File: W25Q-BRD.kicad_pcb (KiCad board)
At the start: 2 copper layers, 16 x 23 mm, 7 parts, among them J1 QSPI, U1 W25Q128JVSIQ

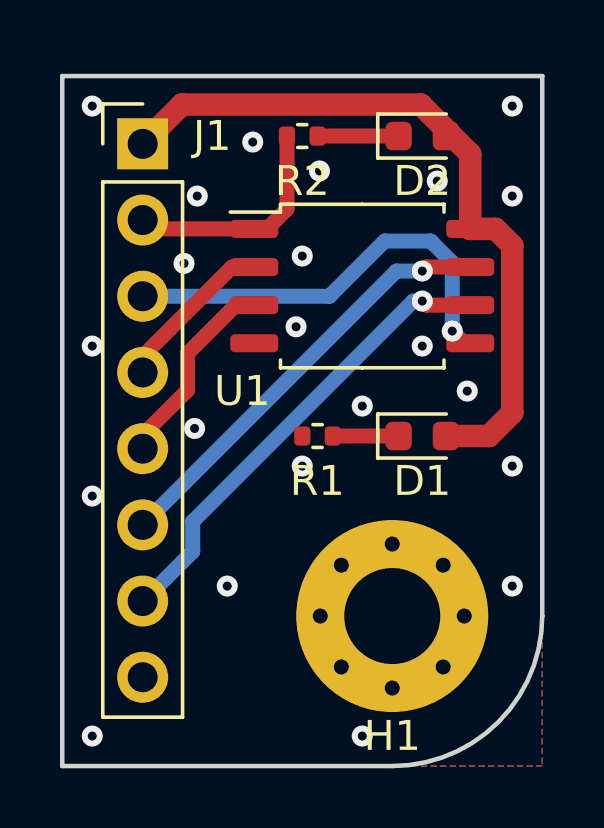
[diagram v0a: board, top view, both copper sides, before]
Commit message: Moved some components around. Generated CAM files.
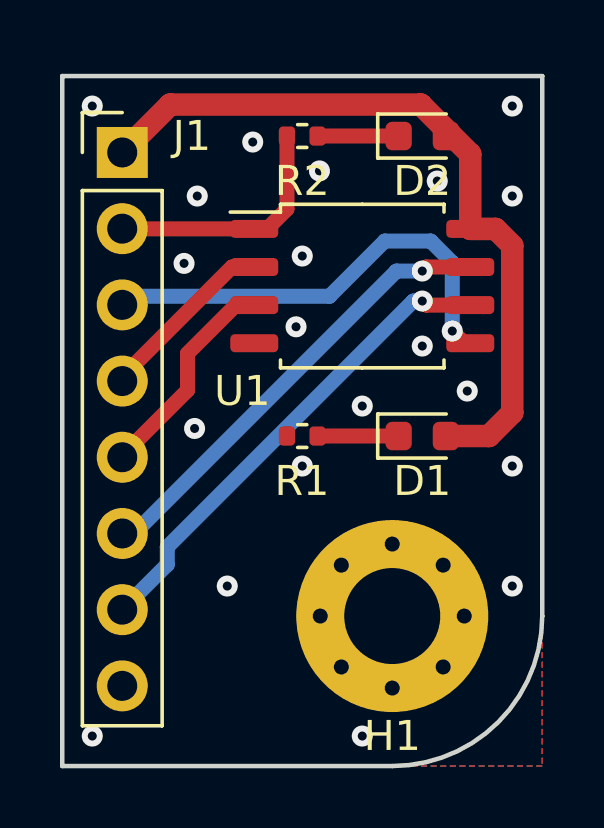
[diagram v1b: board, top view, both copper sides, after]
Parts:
- moved J1 0.74 mm to (133.0, 96.5)
- moved R1 0.51 mm to (139.0, 106.0)
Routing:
- net /IO3: track 14.5 -> 15.3 mm
- net /IO0: track 14.4 -> 15.2 mm
- net +3.3V: track 24.4 -> 25.2 mm
- net /IO1: track 5.49 -> 6.06 mm
- net /IO2: track 6.68 -> 7.25 mm
- net /NCS: track 7.64 -> 8.20 mm
- net /CLK: track 15.7 -> 16.3 mm
- net Net-(D1-Pad1): track 2.19 -> 2.70 mm
- net GND: vias 22 -> 20
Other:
- board text added: "3V3"
- board text added: "CLK"
- board text added: "GND"
- board text added: "IO0"
- board text added: "IO1"
- board text added: "IO2"
- board text added: "IO3"
- board text added: "NCS"
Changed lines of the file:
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@@
   )
   (footprint "Resistor_SMD:R_0402_1005Metric" (layer "F.Cu")
-    (at 139.51 106 180)
+    (at 139 106 180)
     (descr "Resistor SMD 0402 (1005 Metric), square (rectangular) end terminal, IPC_7351 nominal, (Body size source: IPC-SM-782 page 72, https://www.pcb-3d.com/wordpress/wp-content/uploads/ipc-sm-782a_amendment_1_and_2.pdf), generated with kicad-footprint-generator")
     (tags "resistor")
@@
       (effects (font (size 1 1) (thickness 0.15)))
     )
-    (fp_text user "${REFERENCE}" (at 0 0) (layer "F.Fab")
+    (fp_text user "${REFERENCE}" (at 0.51 0) (layer "F.Fab")
       (effects (font (size 0.26 0.26) (thickness 0.04)))
     )
@@
   )
   (footprint "Connector_PinHeader_2.54mm:PinHeader_1x08_P2.54mm_Vertical" (layer "F.Cu")
-    (at 133.68 96.26)
+    (at 133 96.547158)
     (descr "Through hole straight pin header, 1x08, 2.54mm pitch, single row")
     (tags "Through hole pin header THT 1x08 2.54mm single row")
@@
     (property "Sheetname" "")
     (attr through_hole)
-    (fp_text reference "J1" (at 2.32 -0.26) (layer "F.SilkS")
+    (fp_text reference "J1" (at 2.32 -0.547158) (layer "F.SilkS")
       (effects (font (size 1 1) (thickness 0.15)))
     )
@@
   (gr_arc (start 147 112) (mid 145.535534 115.535534) (end 142 117) (layer "Edge.Cuts") (width 0.15))
   (gr_line (start 147 94) (end 131 94) (layer "Edge.Cuts") (width 0.15))
-  (gr_text "${TITLE}\n${COMPANY}" (at 141 102 270) (layer "B.SilkS")
-    (effects (font (size 1 1) (thickness 0.15)) (justify mirror))
-  )
-  (segment (start 142.2125 106) (end 140.02 106) (width 0.5) (layer "F.Cu") (net 1))
-  (segment (start 142.95 94.95) (end 134.99 94.95) (width 0.75) (layer "F.Cu") (net 2))
+  (gr_text "IO2" (at 136 106.707158) (layer "B.SilkS")
+    (effects (font (size 1 1) (thickness 0.15)) (justify mirror))
+  )
+  (gr_text "IO0" (at 136 101.627158) (layer "B.SilkS")
+    (effects (font (size 1 1) (thickness 0.15)) (justify mirror))
+  )
+  (gr_text "NCS" (at 136 99.087158) (layer "B.SilkS")
+    (effects (font (size 1 1) (thickness 0.15)) (justify mirror))
+  )
+  (gr_text "IO3" (at 136 109.247158) (layer "B.SilkS")
+    (effects (font (size 1 1) (thickness 0.15)) (justify mirror))
+  )
+  (gr_text "GND" (at 136 114.327158) (layer "B.SilkS")
+    (effects (font (size 1 1) (thickness 0.15)) (justify mirror))
+  )
+  (gr_text "${TITLE}\n${COMPANY}" (at 144.5 102 90) (layer "B.SilkS")
+    (effects (font (size 1 1) (thickness 0.15)) (justify mirror))
+  )
+  (gr_text "IO1" (at 136 104.167158) (layer "B.SilkS")
+    (effects (font (size 1 1) (thickness 0.15)) (justify mirror))
+  )
+  (gr_text "3V3" (at 136 96.547158) (layer "B.SilkS")
+    (effects (font (size 1 1) (thickness 0.15)) (justify mirror))
+  )
+  (gr_text "CLK" (at 136 111.787158) (layer "B.SilkS")
+    (effects (font (size 1 1) (thickness 0.15)) (justify mirror))
+  )
+  (segment (start 142.2125 106) (end 139.51 106) (width 0.5) (layer "F.Cu") (net 1))
   (segment (start 146 105.225) (end 146 99.65) (width 0.75) (layer "F.Cu") (net 2))
   (segment (start 145.445 99.095) (end 144.6 99.095) (width 0.75) (layer "F.Cu") (net 2))
-  (segment (start 144.6 99.095) (end 144.6 96.6) (width 0.75) (layer "F.Cu") (net 2))
   (segment (start 145.225 106) (end 146 105.225) (width 0.75) (layer "F.Cu") (net 2))
-  (segment (start 134.99 94.95) (end 133.68 96.26) (width 0.75) (layer "F.Cu") (net 2))
+  (segment (start 133 96.547158) (end 134.597158 94.95) (width 0.75) (layer "F.Cu") (net 2))
   (segment (start 146 99.65) (end 145.445 99.095) (width 0.75) (layer "F.Cu") (net 2))
+  (segment (start 144.6 96.6) (end 144.6 99.095) (width 0.75) (layer "F.Cu") (net 2))
+  (segment (start 142.95 94.95) (end 144.6 96.6) (width 0.75) (layer "F.Cu") (net 2))
+  (segment (start 134.597158 94.95) (end 142.95 94.95) (width 0.75) (layer "F.Cu") (net 2))
   (segment (start 143.7875 106) (end 145.225 106) (width 0.75) (layer "F.Cu") (net 2))
-  (segment (start 144.6 96.6) (end 142.95 94.95) (width 0.75) (layer "F.Cu") (net 2))
   (segment (start 142.2125 96) (end 139.51 96) (width 0.5) (layer "F.Cu") (net 3))
   (via (at 143 103) (size 0.7) (drill 0.3) (layers "F.Cu" "B.Cu") (free) (net 4))
@@
   (via (at 146 95) (size 0.7) (drill 0.3) (layers "F.Cu" "B.Cu") (free) (net 4))
   (via (at 144.5 104.5) (size 0.7) (drill 0.3) (layers "F.Cu" "B.Cu") (free) (net 4))
-  (via (at 132 108) (size 0.7) (drill 0.3) (layers "F.Cu" "B.Cu") (free) (net 4))
   (via (at 132 116) (size 0.7) (drill 0.3) (layers "F.Cu" "B.Cu") (free) (net 4))
   (via (at 137.349245 96.200026) (size 0.7) (drill 0.3) (layers "F.Cu" "B.Cu") (free) (net 4))
   (via (at 135.060021 100.245189) (size 0.7) (drill 0.3) (layers "F.Cu" "B.Cu") (free) (net 4))
   (via (at 141 105) (size 0.7) (drill 0.3) (layers "F.Cu" "B.Cu") (free) (net 4))
-  (via (at 132 103) (size 0.7) (drill 0.3) (layers "F.Cu" "B.Cu") (free) (net 4))
   (via (at 143.5 97.5) (size 0.7) (drill 0.3) (layers "F.Cu" "B.Cu") (free) (net 4))
   (via (at 146 107) (size 0.7) (drill 0.3) (layers "F.Cu" "B.Cu") (free) (net 4))
@@
   (segment (start 143 101.5) (end 143.135 101.635) (width 0.5) (layer "F.Cu") (net 5))
   (via (at 143 101.5) (size 0.7) (drill 0.3) (layers "F.Cu" "B.Cu") (net 5))
-  (segment (start 135.35 108.85) (end 135.35 109.85) (width 0.5) (layer "B.Cu") (net 5))
+  (segment (start 134.5 109.7) (end 134.5 110.287158) (width 0.5) (layer "B.Cu") (net 5))
+  (segment (start 134.5 110.287158) (end 133 111.787158) (width 0.5) (layer "B.Cu") (net 5))
+  (segment (start 142.7 101.5) (end 134.5 109.7) (width 0.5) (layer "B.Cu") (net 5))
   (segment (start 143 101.5) (end 142.7 101.5) (width 0.5) (layer "B.Cu") (net 5))
-  (segment (start 133.7 111.5) (end 133.68 111.5) (width 0.5) (layer "B.Cu") (net 5))
-  (segment (start 135.35 109.85) (end 133.7 111.5) (width 0.5) (layer "B.Cu") (net 5))
-  (segment (start 142.7 101.5) (end 135.35 108.85) (width 0.5) (layer "B.Cu") (net 5))
   (segment (start 144 102.5) (end 144.405 102.905) (width 0.5) (layer "F.Cu") (net 6))
   (segment (start 144.405 102.905) (end 144.6 102.905) (width 0.5) (layer "F.Cu") (net 6))
   (via (at 144 102.5) (size 0.7) (drill 0.3) (layers "F.Cu" "B.Cu") (net 6))
+  (segment (start 133.287158 101.34) (end 133 101.627158) (width 0.5) (layer "B.Cu") (net 6))
   (segment (start 143.282843 99.5) (end 141.75 99.5) (width 0.5) (layer "B.Cu") (net 6))
+  (segment (start 144 102.5) (end 144 100.217157) (width 0.5) (layer "B.Cu") (net 6))
   (segment (start 141.75 99.5) (end 139.91 101.34) (width 0.5) (layer "B.Cu") (net 6))
-  (segment (start 139.91 101.34) (end 133.68 101.34) (width 0.5) (layer "B.Cu") (net 6))
   (segment (start 144 100.217157) (end 143.282843 99.5) (width 0.5) (layer "B.Cu") (net 6))
-  (segment (start 144 102.5) (end 144 100.217157) (width 0.5) (layer "B.Cu") (net 6))
-  (segment (start 133.68 103.345) (end 133.68 103.88) (width 0.5) (layer "F.Cu") (net 7))
-  (segment (start 136.66 100.365) (end 133.68 103.345) (width 0.5) (layer "F.Cu") (net 7))
-  (segment (start 137.4 100.365) (end 136.66 100.365) (width 0.5) (layer "F.Cu") (net 7))
-  (segment (start 137.4 101.635) (end 136.79 101.635) (width 0.5) (layer "F.Cu") (net 8))
-  (segment (start 135.175 103.25) (end 135.175 104.475) (width 0.5) (layer "F.Cu") (net 8))
-  (segment (start 136.79 101.635) (end 135.175 103.25) (width 0.5) (layer "F.Cu") (net 8))
-  (segment (start 133.68 105.97) (end 133.68 106.42) (width 0.5) (layer "F.Cu") (net 8))
-  (segment (start 135.175 104.475) (end 133.68 105.97) (width 0.5) (layer "F.Cu") (net 8))
+  (segment (start 139.91 101.34) (end 133.287158 101.34) (width 0.5) (layer "B.Cu") (net 6))
+  (segment (start 136.66 100.365) (end 137.4 100.365) (width 0.5) (layer "F.Cu") (net 7))
+  (segment (start 133 104.025) (end 136.66 100.365) (width 0.5) (layer "F.Cu") (net 7))
+  (segment (start 133 104.167158) (end 133 104.025) (width 0.5) (layer "F.Cu") (net 7))
+  (segment (start 136.79 101.635) (end 137.4 101.635) (width 0.5) (layer "F.Cu") (net 8))
+  (segment (start 135.175 104.475) (end 135.175 103.25) (width 0.5) (layer "F.Cu") (net 8))
+  (segment (start 133 106.707158) (end 133 106.65) (width 0.5) (layer "F.Cu") (net 8))
+  (segment (start 133 106.65) (end 135.175 104.475) (width 0.5) (layer "F.Cu") (net 8))
+  (segment (start 135.175 103.25) (end 136.79 101.635) (width 0.5) (layer "F.Cu") (net 8))
   (segment (start 143.135 100.365) (end 144.6 100.365) (width 0.5) (layer "F.Cu") (net 9))
   (segment (start 143 100.5) (end 143.135 100.365) (width 0.5) (layer "F.Cu") (net 9))
   (via (at 143 100.5) (size 0.7) (drill 0.3) (layers "F.Cu" "B.Cu") (net 9))
-  (segment (start 142.14 100.5) (end 133.68 108.96) (width 0.5) (layer "B.Cu") (net 9))
+  (segment (start 142.14 100.5) (end 133.392842 109.247158) (width 0.5) (layer "B.Cu") (net 9))
+  (segment (start 133.392842 109.247158) (end 133 109.247158) (width 0.5) (layer "B.Cu") (net 9))
   (segment (start 143 100.5) (end 142.14 100.5) (width 0.5) (layer "B.Cu") (net 9))
   (segment (start 138.49 98.435) (end 137.83 99.095) (width 0.5) (layer "F.Cu") (net 10))
-  (segment (start 137.4 99.095) (end 133.975 99.095) (width 0.5) (layer "F.Cu") (net 10))
-  (segment (start 133.975 99.095) (end 133.68 98.8) (width 0.5) (layer "F.Cu") (net 10))
+  (segment (start 137.4 99.095) (end 133.007842 99.095) (width 0.5) (layer "F.Cu") (net 10))
   (segment (start 137.83 99.095) (end 137.4 99.095) (width 0.5) (layer "F.Cu") (net 10))
   (segment (start 138.49 96) (end 138.49 98.435) (width 0.5) (layer "F.Cu") (net 10))
+  (segment (start 133.007842 99.095) (end 133 99.087158) (width 0.5) (layer "F.Cu") (net 10))
   (zone (net 4) (net_name "GND") (layers F&B.Cu) (hatch edge 0.508)
     (connect_pads yes (clearance 0.508))

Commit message: Version 1.1. Added 2 caps. Added few texts.
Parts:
- added C1: 100nF, Capacitor_SMD:C_0402_1005Metric, F.Cu at (144.5, 96.0)
- added C2: 1uF, Capacitor_SMD:C_0603_1608Metric, F.Cu at (144.5, 106.0)
- moved D1 2.00 mm to (141.0, 106.0)
- moved D2 2.00 mm to (141.0, 96.0)
- moved R1 1.50 mm to (137.5, 106.0)
- moved R2 1.50 mm to (137.5, 96.0)
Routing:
- net +3.3V: track 25.2 -> 26.4 mm
- net /NCS: track 8.20 -> 7.67 mm
- net Net-(D2-Pad1): track 2.70 -> 2.20 mm
- net Net-(D1-Pad1): track 2.70 -> 2.20 mm
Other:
- board text added: "+"
- board text added: "ACT"
- board text added: "PWR"
